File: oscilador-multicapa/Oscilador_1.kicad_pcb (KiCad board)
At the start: 4 copper layers, 24 x 19.5 mm, 20 parts, among them J201 Conn_01x02, Q301 BC546, Q302 BC546, U201 40106

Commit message: Ejercicio terminado multicapa.
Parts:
- added F1: Fiducial, Fiducial:Fiducial_1mm_Dia_2mm_Outer, B.Cu at (145.5, 95.5)
- added F2: Fiducial, Fiducial:Fiducial_1mm_Dia_2mm_Outer, F.Cu at (145.5, 80.5)
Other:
- board text added: "IND. ARG."
- board text added: "KiCad Escuela MC"
- board text added: "Mínimos (Mayer 10 mils): Grillas: 1mm, 0,5mm, 0,25mm Vía: 1 mm / 0,5 mm Márgen: 0,25 mm Pista: 0,25 mm Dist. a borde: 0,3 mm Terminación: HASL"
- board text added: "V092018"
- board text removed: "Mínimos (Mayer 10 mils): Vía: 1 mm / 0,5 mm Márgen: 0,25 mm Pista: 0,25 mm Dist. a borde: 0,3 mm"
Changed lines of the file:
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@@
   (general
     (thickness 1.6)
-    (drawings 13)
+    (drawings 16)
     (tracks 93)
     (zones 0)
-    (modules 20)
+    (modules 22)
     (nets 15)
   )
@@
   (title_block
     (title "Ejercicio KICAD Multicapa")
-    (date 2018-09-16)
+    (date 2018-09-28)
     (rev 1)
     (company "Diego Brengi - Cursos KiCad")
@@
   (layers
     (0 F.Cu signal)
-    (1 In1.Cu.GND power)
-    (2 In2.Cu.VCC jumper)
+    (1 In1.Cu.GND power hide)
+    (2 In2.Cu.VCC jumper hide)
     (31 B.Cu signal)
     (32 B.Adhes user)
     (33 F.Adhes user)
     (34 B.Paste user hide)
-    (35 F.Paste user)
+    (35 F.Paste user hide)
     (36 B.SilkS user)
     (37 F.SilkS user)
@@
     (pad_drill 0.6)
     (pad_to_mask_clearance 0.2)
-    (aux_axis_origin 142 95.5)
-    (grid_origin 142 95.5)
-    (visible_elements FFFDFF3F)
+    (aux_axis_origin 145.5 95.5)
+    (grid_origin 145.5 95.5)
+    (visible_elements FFFDFF7F)
     (pcbplotparams
       (layerselection 0x010fc_ffffffff)
@@
     (add_net "Net-(Q302-Pad2)")
   )
+  (module Fiducial:Fiducial_1mm_Dia_2mm_Outer (layer F.Cu)
+    (at 145.5 80.5)
+    (descr "Circular Fiducial, 1mm bare copper top; 2mm keepout (Level A)")
+    (tags marker)
+    (attr virtual)
+    (fp_text reference F2 (at 0 -2) (layer F.SilkS) hide
+      (effects (font (size 1 1) (thickness 0.15)))
+    )
+    (fp_text value Fiducial (at 0 2) (layer F.Fab)
+      (effects (font (size 1 1) (thickness 0.15)))
+    )
+    (fp_circle (center 0 0) (end 1 0) (layer F.Fab) (width 0.1))
+    (fp_text user %R (at 0 0) (layer F.Fab)
+      (effects (font (size 0.4 0.4) (thickness 0.06)))
+    )
+    (fp_circle (center 0 0) (end 1.25 0) (layer F.CrtYd) (width 0.05))
+    (pad ~ smd circle (at 0 0) (size 1 1) (layers F.Cu F.Mask)
+      (solder_mask_margin 0.5) (clearance 0.5))
+  )
+  (module Fiducial:Fiducial_1mm_Dia_2mm_Outer (layer B.Cu)
+    (at 145.5 95.5)
+    (descr "Circular Fiducial, 1mm bare copper top; 2mm keepout (Level A)")
+    (tags marker)
+    (attr virtual)
+    (fp_text reference F1 (at 0 2) (layer B.SilkS) hide
+      (effects (font (size 1 1) (thickness 0.15)) (justify mirror))
+    )
+    (fp_text value Fiducial (at 0 -2) (layer B.Fab)
+      (effects (font (size 1 1) (thickness 0.15)) (justify mirror))
+    )
+    (fp_circle (center 0 0) (end 1 0) (layer B.Fab) (width 0.1))
+    (fp_text user %R (at 0 0) (layer B.Fab)
+      (effects (font (size 0.4 0.4) (thickness 0.06)) (justify mirror))
+    )
+    (fp_circle (center 0 0) (end 1.25 0) (layer B.CrtYd) (width 0.05))
+    (pad ~ smd circle (at 0 0) (size 1 1) (layers B.Cu B.Mask)
+      (solder_mask_margin 0.5) (clearance 0.5))
+  )
   (module Capacitor_Tantalum_SMD:CP_EIA-2012-12_Kemet-R_Pad1.30x1.05mm_HandSolder (layer F.Cu)
     (at 148.5 85.5 270)
@@
     (tags "SOIC 1.27")
     (attr smd)
-    (fp_text reference U201 (at 0 -5.375) (layer F.SilkS)
-      (effects (font (size 1 1) (thickness 0.15)))
+    (fp_text reference U201 (at -1.25 -6 180) (layer F.SilkS)
+      (effects (font (size 0.8 0.8) (thickness 0.15)))
     )
     (fp_text value 40106 (at 0 5.375) (layer F.Fab)
@@
     )
   )
+  (gr_text V092018 (at 162 88.75 90) (layer B.SilkS)
+    (effects (font (size 1.2 1.2) (thickness 0.3)) (justify mirror))
+  )
+  (gr_text "KiCad Escuela MC" (at 151.5 96.5) (layer F.SilkS)
+    (effects (font (size 1.1 1.1) (thickness 0.25)))
+  )
+  (gr_text "IND. ARG." (at 151 80) (layer B.Cu)
+    (effects (font (size 1.2 1.2) (thickness 0.3)) (justify mirror))
+  )
   (gr_text "Ejercicio KiCad Multicapa" (at 130.5 67.75) (layer Dwgs.User)
     (effects (font (size 2 2) (thickness 0.4)) (justify left))
@@
   (gr_line (start 151 89.75) (end 150 90.5) (layer F.SilkS) (width 0.2))
   (gr_line (start 151 89.25) (end 151 89.75) (layer F.SilkS) (width 0.2))
-  (gr_text "Mínimos (Mayer 10 mils): \nVía: 1 mm / 0,5 mm\nMárgen: 0,25 mm\nPista: 0,25 mm\nDist. a borde: 0,3 mm" (at 167.5 89) (layer Dwgs.User)
+  (gr_text "Mínimos (Mayer 10 mils): \nGrillas: 1mm, 0,5mm, 0,25mm\nVía: 1 mm / 0,5 mm\nMárgen: 0,25 mm\nPista: 0,25 mm\nDist. a borde: 0,3 mm\nTerminación: HASL" (at 167.5 89) (layer Dwgs.User)
     (effects (font (size 1.5 1.5) (thickness 0.3)) (justify left))
   )
@@
   )
   (zone (net 3) (net_name +5V) (layer In2.Cu.VCC) (hatch edge 0.508)
-    (connect_pads (clearance 0.5))
-    (min_thickness 0.5)
+    (connect_pads (clearance 0.3))
+    (min_thickness 0.3)
     (fill yes (arc_segments 16) (thermal_gap 0.5) (thermal_bridge_width 0.55))
     (polygon
@@
       )
     )
+  )
+  (zone (net 0) (net_name "") (layer B.Mask) (hatch edge 0.508)
+    (connect_pads (clearance 0.508))
+    (min_thickness 0.254)
+    (fill yes (arc_segments 16) (thermal_gap 0.508) (thermal_bridge_width 0.508))
+    (polygon
+      (pts
+        (xy 146.5 78.75) (xy 155.5 78.75) (xy 155.5 81) (xy 146.5 81)
+      )
+    )

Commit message: Agrego verificador de capas.
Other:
- board text added: "IND.ARG."
- board text added: "[ 2 ]"
- board text added: "[ 3 ]"
- board text added: "[ 4]"
- board text added: "[1 ]"
- board text removed: "IND. ARG."
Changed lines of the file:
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@@
   (general
     (thickness 1.6)
-    (drawings 16)
+    (drawings 20)
     (tracks 93)
     (zones 0)
@@
   (layers
     (0 F.Cu signal)
-    (1 In1.Cu.GND power hide)
-    (2 In2.Cu.VCC jumper hide)
+    (1 In1.Cu.GND power)
+    (2 In2.Cu.VCC jumper)
     (31 B.Cu signal)
     (32 B.Adhes user)
@@
     (36 B.SilkS user)
     (37 F.SilkS user)
-    (38 B.Mask user hide)
+    (38 B.Mask user)
     (39 F.Mask user hide)
     (40 Dwgs.User user)
@@
     )
   )
+  (gr_text "[   4]" (at 154 80) (layer B.Cu)
+    (effects (font (size 1 1) (thickness 0.25)) (justify left))
+  )
+  (gr_text "[  3 ]" (at 154 80) (layer In2.Cu.VCC)
+    (effects (font (size 1 1) (thickness 0.25)) (justify left))
+  )
+  (gr_text "[ 2  ]" (at 154 80) (layer In1.Cu.GND)
+    (effects (font (size 1 1) (thickness 0.25)) (justify left))
+  )
+  (gr_text "[1   ]" (at 154 80) (layer F.Cu)
+    (effects (font (size 1 1) (thickness 0.25)) (justify left))
+  )
   (gr_text V092018 (at 162 88.75 90) (layer B.SilkS)
     (effects (font (size 1.2 1.2) (thickness 0.3)) (justify mirror))
@@
     (effects (font (size 1.1 1.1) (thickness 0.25)))
   )
-  (gr_text "IND. ARG." (at 151 80) (layer B.Cu)
+  (gr_text IND.ARG. (at 150.25 80) (layer B.Cu)
     (effects (font (size 1.2 1.2) (thickness 0.3)) (justify mirror))
   )
@@
     (polygon
       (pts
-        (xy 146.5 78.75) (xy 155.5 78.75) (xy 155.5 81) (xy 146.5 81)
+        (xy 146.5 78.75) (xy 154 78.75) (xy 154 81) (xy 146.5 81)
       )
     )

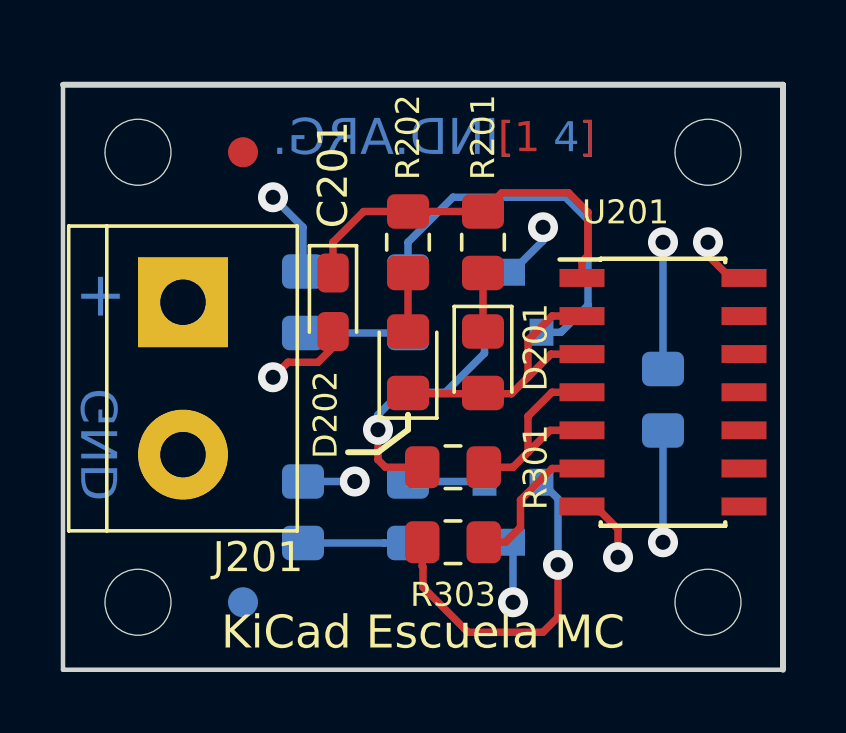
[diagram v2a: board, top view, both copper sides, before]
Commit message: Detalles de grilla, agrego margen, agrego notas de stackup, Corrección errores de DRC por cerca.
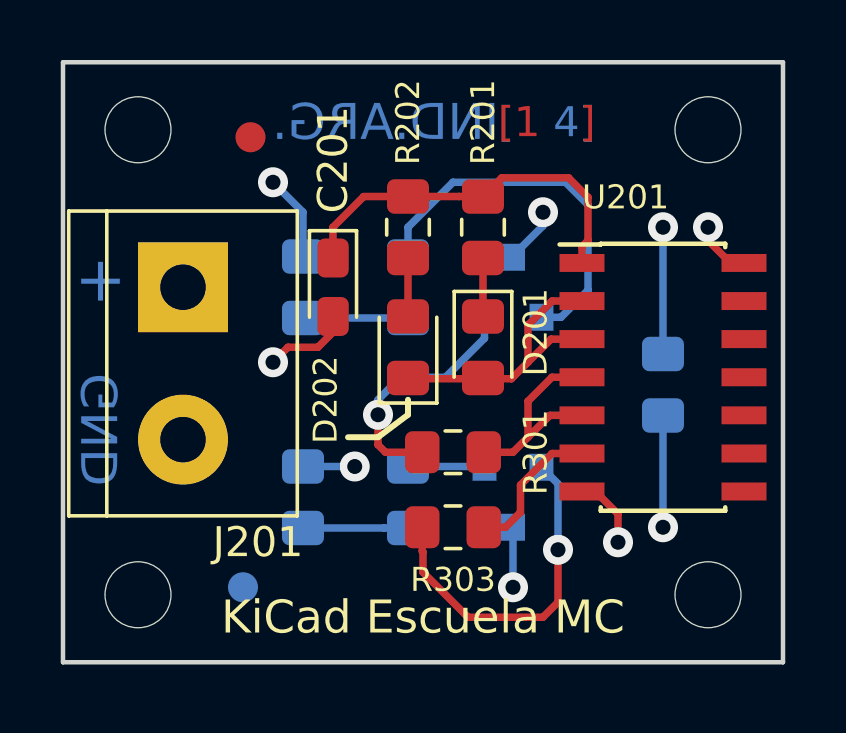
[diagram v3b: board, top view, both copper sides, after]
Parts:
- moved MK101 0.75 mm to (161.0, 79.8)
- moved MK104 0.75 mm to (142.0, 79.8)
- moved F2 0.56 mm to (145.8, 80.0)
- moved C201 0.50 mm to (148.5, 85.0)
- moved C202 0.50 mm to (159.5, 88.2)
- moved D201 0.50 mm to (153.5, 87.0)
- moved D202 0.50 mm to (151.0, 87.0)
- moved D301 0.50 mm to (151.0, 85.0)
- moved D302 0.50 mm to (151.0, 92.0)
- moved F1 0.50 mm to (145.5, 95.0)
- moved J201 0.50 mm to (143.5, 85.0)
- moved Q301 0.50 mm to (154.5, 85.0)
- moved Q302 0.50 mm to (154.5, 92.0)
- moved R201 0.50 mm to (153.5, 83.0)
- moved R202 0.50 mm to (151.0, 83.0)
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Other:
- board size 24 x 19.5 mm -> 24 x 20 mm
- board text added: "1 - Signal"
- board text added: "1oz"
- board text added: "2 - GND"
- board text added: "3 - Power"
- board text added: "4 - Signal"
- board text added: "Material/espesor"
- board text added: "STACKUP"
